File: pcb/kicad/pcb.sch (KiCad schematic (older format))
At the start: 4 parts

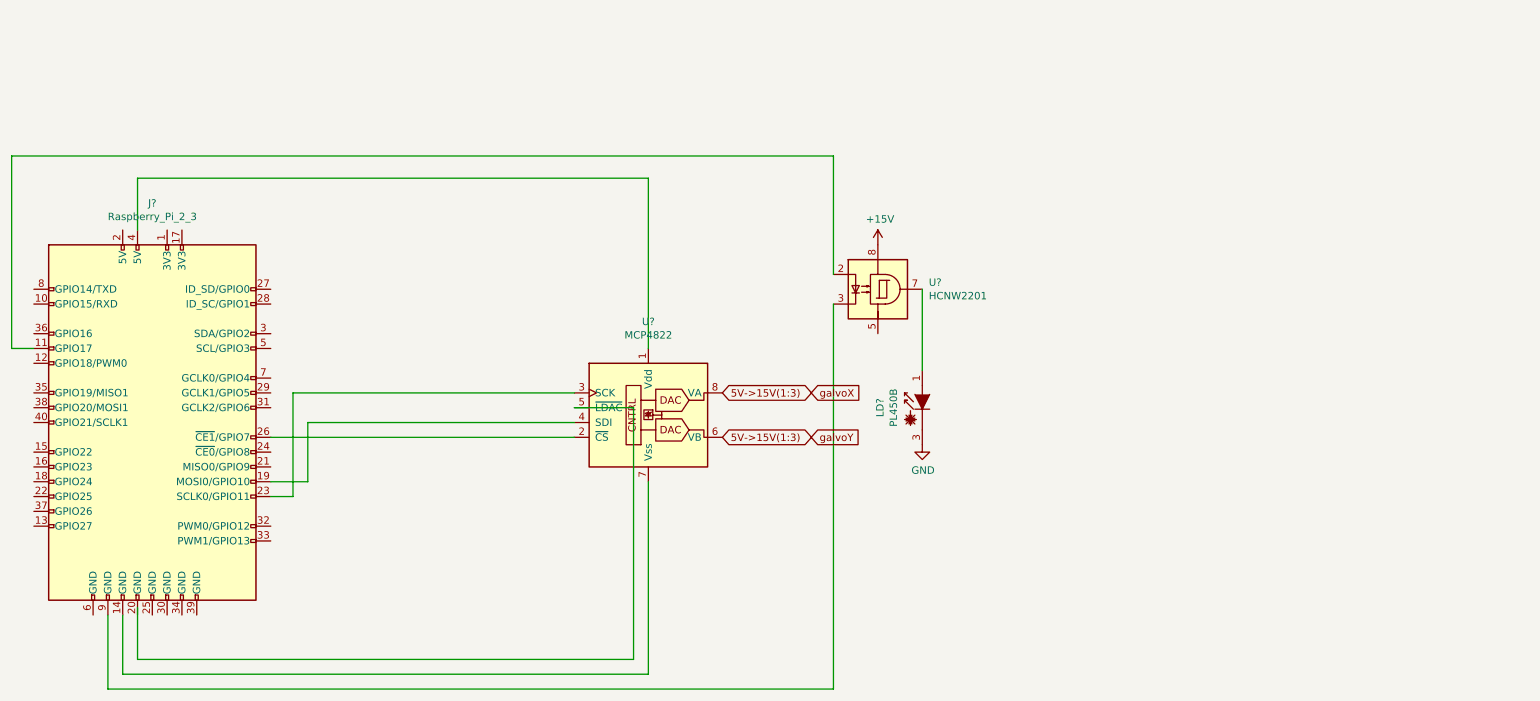
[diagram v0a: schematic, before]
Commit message: add web_ui ilda file select menu
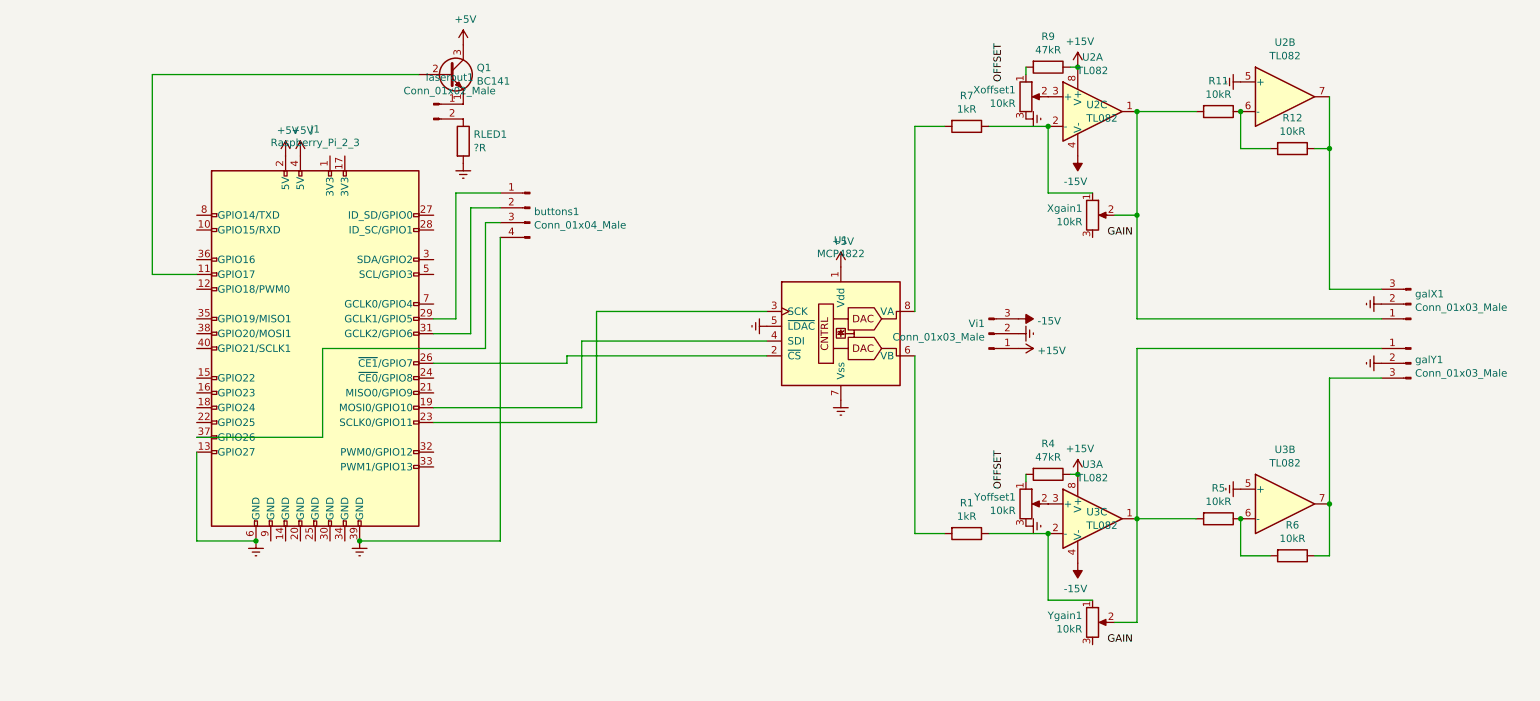
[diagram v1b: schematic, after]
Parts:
- removed J?: Raspberry_Pi_2_3, symbol Connector:Raspberry_Pi_2_3
- removed LD?: PL450B, OptoDevice:LaserDiode_TO38ICut-3, symbol Diode_Laser:PL450B
- removed U?: MCP4822, symbol Analog_DAC:MCP4822
- removed U?: HCNW2201, Package_DIP:DIP-8_W10.16mm, symbol Isolator:HCNW2201
- added J1: Raspberry_Pi_2_3, Connector_PinSocket_2.54mm:PinSocket_2x20_P2.54mm_Vertical, symbol Connector:Raspberry_Pi_2_3
- added Q1: BC141, Package_TO_SOT_THT:TO-39-3, symbol Transistor_BJT:BC141
- added R1, R7: 1kR, Resistor_THT:R_Axial_DIN0207_L6.3mm_D2.5mm_P10.16mm_Horizontal, symbol Device:R
- added R11, R12, R5, R6: 10kR, Resistor_THT:R_Axial_DIN0207_L6.3mm_D2.5mm_P10.16mm_Horizontal, symbol Device:R
- added R4, R9: 47kR, Resistor_THT:R_Axial_DIN0207_L6.3mm_D2.5mm_P10.16mm_Horizontal, symbol Device:R
- added RLED1: ?R, Resistor_THT:R_Axial_DIN0207_L6.3mm_D2.5mm_P10.16mm_Horizontal, symbol Device:R
- added U1: MCP4822, Package_DIP:DIP-8_W7.62mm, symbol Analog_DAC:MCP4822
- added U2, U3: TL082, Package_DIP:DIP-8_W7.62mm, symbol Amplifier_Operational:TL082
- added Vi1, galX1, galY1: Conn_01x03_Male, Connector_PinHeader_2.54mm:PinHeader_1x03_P2.54mm_Horizontal, symbol Connector:Conn_01x03_Male
- added Xgain1, Xoffset1, Ygain1, Yoffset1: 10kR, Potentiometer_THT:Potentiometer_Alps_RK09Y11_Single_Horizontal, symbol Device:R_POT
- added buttons1: Conn_01x04_Male, Connector_PinHeader_2.54mm:PinHeader_1x04_P2.54mm_Horizontal, symbol Connector:Conn_01x04_Male
- added laserout1: Conn_01x02_Male, Connector_PinHeader_2.54mm:PinHeader_1x02_P2.54mm_Horizontal, symbol Connector:Conn_01x02_Male
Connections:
- net labels added: +5V, -15V, Earth, GAIN, OFFSET
- net labels removed: 5V->15V(1:3), GND, galvoX, galvoY
- wire segments 25 -> 63
